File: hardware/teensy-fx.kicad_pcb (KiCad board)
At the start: 2 copper layers, 17 parts, among them J1 AudioJack3_Ground, J2 AudioJack3_Ground, U1 Teensy4.0, U2 AP7313-1.8V, U3 SGTL5000

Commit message: initial schematic and parts layout
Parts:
- added C10: 2.2u, Capacitor_SMD:C_0805_2012Metric, F.Cu at (266.1, 69.0)
- added D1: LED, LED_SMD:LED_0805_2012Metric, F.Cu at (238.1, 90.0)
- added D10: LED, LED_SMD:LED_0805_2012Metric, F.Cu at (253.1, 126.0)
- added D11: LED, LED_SMD:LED_0805_2012Metric, F.Cu at (268.1, 126.0)
- added D12: LED, LED_SMD:LED_0805_2012Metric, F.Cu at (283.0, 126.0)
- added D13: LED, LED_SMD:LED_0805_2012Metric, F.Cu at (277.0, 79.0)
- added D14: LED, LED_SMD:LED_0805_2012Metric, F.Cu at (233.0, 79.0)
- added D15: LED, LED_SMD:LED_0805_2012Metric, F.Cu at (261.1, 79.0)
- added D16: LED, LED_SMD:LED_0805_2012Metric, F.Cu at (247.9, 79.0)
- added D2: LED, LED_SMD:LED_0805_2012Metric, F.Cu at (253.0, 90.0)
- added D3: LED, LED_SMD:LED_0805_2012Metric, F.Cu at (268.0, 90.0)
- added D4: LED, LED_SMD:LED_0805_2012Metric, F.Cu at (283.0, 90.0)
- added D5: LED, LED_SMD:LED_0805_2012Metric, F.Cu at (238.0, 108.0)
- added D6: LED, LED_SMD:LED_0805_2012Metric, F.Cu at (253.0, 108.0)
- added D7: LED, LED_SMD:LED_0805_2012Metric, F.Cu at (268.0, 108.0)
- added D8: LED, LED_SMD:LED_0805_2012Metric, F.Cu at (283.0, 108.0)
- added D9: LED, LED_SMD:LED_0805_2012Metric, F.Cu at (238.0, 126.0)
- added H1: MountingHole, MountingHole:MountingHole_3.2mm_M3, F.Cu at (230.0, 50.0)
- added H2: MountingHole, MountingHole:MountingHole_3.2mm_M3, F.Cu at (280.0, 50.0)
- added H3: MountingHole, MountingHole:MountingHole_3.2mm_M3, F.Cu at (230.0, 145.0)
- added H4: MountingHole, MountingHole:MountingHole_3.2mm_M3, F.Cu at (280.0, 145.0)
- added R3: R, Resistor_SMD:R_0805_2012Metric, F.Cu at (257.0, 49.4)
- added R4: 10k, Resistor_SMD:R_0805_2012Metric, F.Cu at (262.0, 50.0)
- added RN1: R_Pack04, Resistor_SMD:R_Array_Concave_4x0603, F.Cu at (243.0, 90.0)
- added RN2: R_Pack04, Resistor_SMD:R_Array_Concave_4x0603, F.Cu at (243.0, 125.0)
- added RN3: R_Pack04, Resistor_SMD:R_Array_Concave_4x0603, F.Cu at (243.0, 78.0)
- added RN4: R_Pack04, Resistor_SMD:R_Array_Concave_4x0603, F.Cu at (243.0, 108.0)
- added RV1: R_POT, Potentiometer_THT:Potentiometer_Alps_RK09L_Single_Vertical, F.Cu at (235.0, 104.0)
- added RV10: R_POT, Potentiometer_THT:Potentiometer_Alps_RK09L_Single_Vertical, F.Cu at (250.0, 140.0)
- added RV11: R_POT, Potentiometer_THT:Potentiometer_Alps_RK09L_Single_Vertical, F.Cu at (265.0, 140.0)
- added RV12: R_POT, Potentiometer_THT:Potentiometer_Alps_RK09L_Single_Vertical, F.Cu at (280.0, 140.0)
- added RV2: R_POT, Potentiometer_THT:Potentiometer_Alps_RK09L_Single_Vertical, F.Cu at (250.0, 104.0)
- added RV3: R_POT, Potentiometer_THT:Potentiometer_Alps_RK09L_Single_Vertical, F.Cu at (265.0, 104.0)
- added RV4: R_POT, Potentiometer_THT:Potentiometer_Alps_RK09L_Single_Vertical, F.Cu at (280.0, 104.0)
- added RV5: R_POT, Potentiometer_THT:Potentiometer_Alps_RK09L_Single_Vertical, F.Cu at (235.0, 122.0)
- added RV6: R_POT, Potentiometer_THT:Potentiometer_Alps_RK09L_Single_Vertical, F.Cu at (250.0, 122.0)
- added RV7: R_POT, Potentiometer_THT:Potentiometer_Alps_RK09L_Single_Vertical, F.Cu at (265.0, 122.0)
- added RV8: R_POT, Potentiometer_THT:Potentiometer_Alps_RK09L_Single_Vertical, F.Cu at (280.0, 122.0)
- added RV9: R_POT, Potentiometer_THT:Potentiometer_Alps_RK09L_Single_Vertical, F.Cu at (235.0, 140.0)
- added SW1: Switch_SW_Push, Button_Switch_THT:SW_PUSH_6mm, F.Cu at (230.0, 82.0)
- added SW2: Switch_SW_Push, Button_Switch_THT:SW_PUSH_6mm, F.Cu at (244.0, 82.0)
- added SW3: Switch_SW_Push, Button_Switch_THT:SW_PUSH_6mm, F.Cu at (258.0, 82.0)
- added SW4: Switch_SW_Push, Button_Switch_THT:SW_PUSH_6mm, F.Cu at (274.0, 82.0)
- added U4: 4067, Package_SO:SSOP-24_5.3x8.2mm_P0.65mm, F.Cu at (273.0, 71.0)
- added U5: 74HC595, Package_SO:QSOP-16_3.9x4.9mm_P0.635mm, F.Cu at (255.0, 145.0)
- added U6: 74HC595, Package_SO:QSOP-16_3.9x4.9mm_P0.635mm, F.Cu at (255.0, 76.0)
- J1, J2: moved to B.Cu
- moved J1 135.4 mm to (279.0, 60.0), turned to 90 degrees
- moved U3 126.8 mm to (266.0, 58.0)
- moved U1 100.2 mm to (243.0, 63.0)
- moved C6 84.4 mm to (254.7, 59.3)
- moved C9 84.4 mm to (254.7, 62.2)
- moved L1 84.4 mm to (259.1, 59.3)
- moved R2 84.4 mm to (259.1, 62.2)
- moved C3 83.6 mm to (245.9, 49.7), turned to 90 degrees
- moved C1 80.7 mm to (243.9, 49.7), turned to 90 degrees
- moved U2 75.9 mm to (240.2, 49.7), turned to 90 degrees
- moved J2 75.8 mm to (231.0, 62.0), turned to 270 degrees
- moved C2 68.6 mm to (240.8, 64.4)
- moved C4 68.6 mm to (240.8, 67.3)
- moved C5 68.6 mm to (245.2, 64.4)
- moved C7 68.6 mm to (245.2, 67.3)
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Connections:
- net Net-(U1-Pad33) renamed +5V
- U1 pad 10: Net-(U1-Pad10) -> TX
- U1 pad 11: Net-(U1-Pad11) -> led_data
- U1 pad 12: Net-(U1-Pad12) -> led_clk
- U1 pad 13: Net-(U1-Pad13) -> led_latch
- U1 pad 14: Net-(U1-Pad14) -> led_oe
- U1 pad 2: Net-(U1-Pad2) -> sw_1
- U1 pad 20: Net-(U1-Pad20) -> sw_4
- U1 pad 21: Net-(U1-Pad21) -> pot_multiplex
- U1 pad 23: Net-(U1-Pad23) -> SCL
- U1 pad 24: Net-(U1-Pad24) -> SDA
- U1 pad 27: Net-(U1-Pad27) -> LRCLK
- U1 pad 28: Net-(U1-Pad28) -> BCLK
- U1 pad 3: Net-(U1-Pad3) -> sw_2
- U1 pad 31: Net-(U1-Pad31) -> +3V3
- U1 pad 32: Net-(U1-Pad32) -> GND
- U1 pad 4: Net-(U1-Pad4) -> pot_b0
- U1 pad 5: Net-(U1-Pad5) -> pot_b1
- U1 pad 6: Net-(U1-Pad6) -> pot_b2
- U1 pad 7: Net-(U1-Pad7) -> pot_b3
- U1 pad 8: Net-(U1-Pad8) -> sw_3
- U1 pad 9: Net-(U1-Pad9) -> RX
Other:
- board outline added: 60 x 105 mm

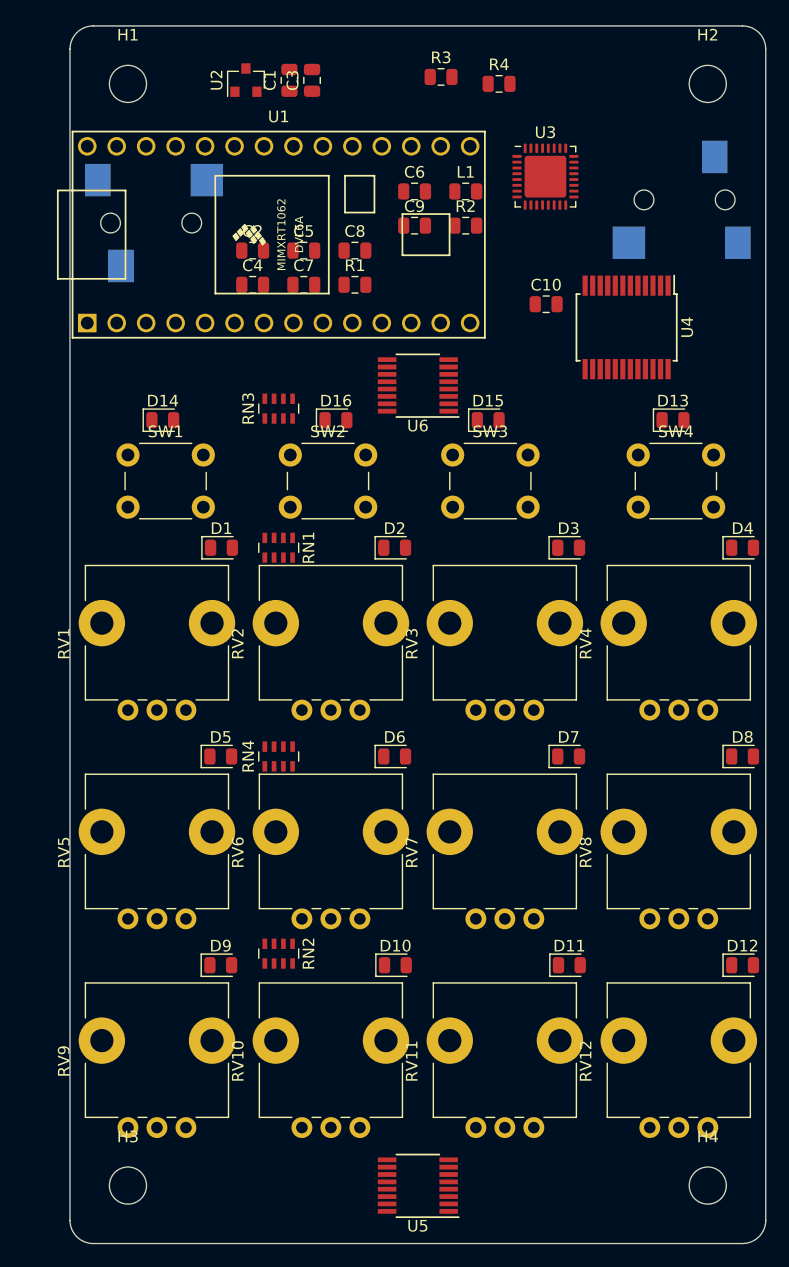
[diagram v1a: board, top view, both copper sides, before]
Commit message: switch to pwm led driver, first pass routing
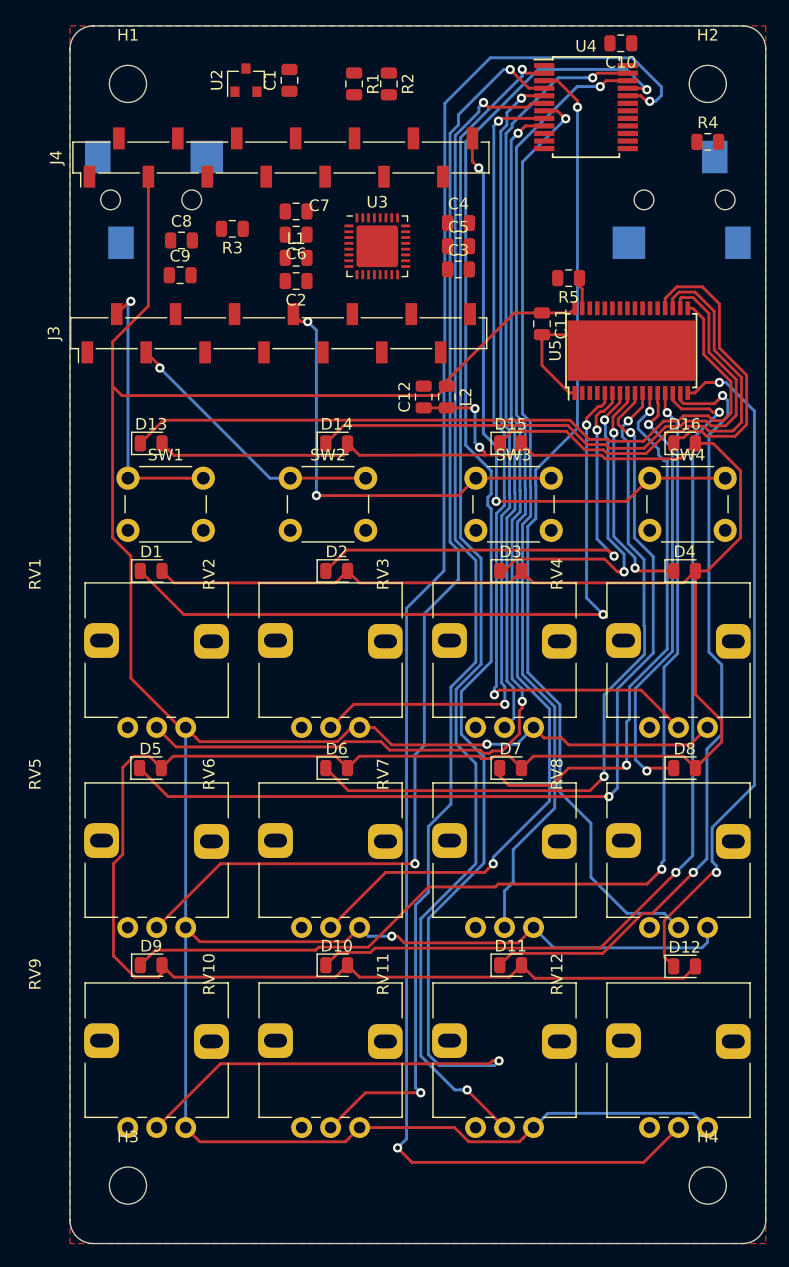
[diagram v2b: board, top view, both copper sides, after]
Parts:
- removed RN1, RN2, RN3, RN4: R_Pack04, Resistor_SMD:R_Array_Concave_4x0603
- removed U1: Teensy4.0, teensy:Teensy40
- removed U6: 74HC595, Package_SO:QSOP-16_3.9x4.9mm_P0.635mm
- added C11: 2.2uF, Capacitor_SMD:C_0805_2012Metric, F.Cu at (265.7, 70.7)
- added C12: 2.2uF, Capacitor_SMD:C_0805_2012Metric, F.Cu at (255.5, 77.0)
- added J3: Conn_01x14, Connector_PinSocket_2.54mm:PinSocket_1x14_P2.54mm_Vertical_SMD_Pin1Left, F.Cu at (243.0, 71.5)
- added J4: Conn_01x14, Connector_PinSocket_2.54mm:PinSocket_1x14_P2.54mm_Vertical_SMD_Pin1Left, F.Cu at (243.2, 56.4)
- added L2: 600R, Inductor_SMD:L_0805_2012Metric, F.Cu at (257.5, 77.0)
- added R5: 3.3k, Resistor_SMD:R_0805_2012Metric, F.Cu at (268.0, 66.8)
- C10: value 2.2u -> 2.2uF
- R3: value R -> 100R
- RV1, RV10, RV11, RV12, RV2, RV3, RV4, RV5, RV6, RV7, RV8, RV9: footprint Potentiometer_THT:Potentiometer_Alps_RK09L_Single_Vertical -> audio-fx:Potentiometer_Alps_RK09L_Single_Vertical
- U5: value 74HC595 -> TLC5947DAP; footprint Package_SO:QSOP-16_3.9x4.9mm_P0.635mm -> Package_SO:HTSSOP-32-1EP_6.1x11mm_P0.65mm_EP5.2x11mm_Mask4.11x4.36mm
- moved U5 74.3 mm to (273.4, 73.0), turned to 90 degrees
- moved J2 48.0 mm to (279.0, 60.0), turned to 90 degrees
- moved J1 48.0 mm to (231.0, 60.0), turned to 270 degrees
- moved D13 45.0 mm to (232.0, 81.0)
- moved D16 30.1 mm to (278.0, 81.0)
- moved C10 23.4 mm to (272.5, 46.5), turned to 180 degrees
- moved R3 22.3 mm to (239.0, 62.5), turned to 180 degrees
- moved C9 20.7 mm to (234.5, 66.5)
- moved C3 20.6 mm to (258.5, 66.0), turned to 0 degrees
- moved U4 19.3 mm to (269.5, 52.0), turned to 0 degrees
- moved R4 18.7 mm to (280.0, 55.0)
- moved C4 18.5 mm to (258.5, 62.0)
- moved R1 17.3 mm to (249.5, 50.0), turned to 270 degrees
- moved L1 15.7 mm to (244.5, 65.0)
- moved U3 15.7 mm to (251.5, 64.0)
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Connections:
- D1 pad 1: GND -> Net-(D1-Pad1)
- D1 pad 2: /pots/led_0 -> +3.3VA
- D10 pad 1: GND -> Net-(D10-Pad1)
- D10 pad 2: /pots/led_13 -> +3.3VA
- D11 pad 1: GND -> Net-(D11-Pad1)
- D11 pad 2: /pots/led_14 -> +3.3VA
- D12 pad 1: GND -> Net-(D12-Pad1)
- D12 pad 2: /pots/led_15 -> +3.3VA
- D13 pad 1: GND -> Net-(D13-Pad1)
- D13 pad 2: /pots/led_8 -> +3.3VA
- D14 pad 1: GND -> Net-(D14-Pad1)
- D14 pad 2: /pots/led_9 -> +3.3VA
- D15 pad 1: GND -> Net-(D15-Pad1)
- D15 pad 2: /pots/led_10 -> +3.3VA
- D16 pad 1: GND -> Net-(D16-Pad1)
- D16 pad 2: /pots/led_11 -> +3.3VA
- D2 pad 1: GND -> Net-(D2-Pad1)
- D2 pad 2: /pots/led_1 -> +3.3VA
- D3 pad 1: GND -> Net-(D3-Pad1)
- D3 pad 2: /pots/led_2 -> +3.3VA
- D4 pad 1: GND -> Net-(D4-Pad1)
- D4 pad 2: /pots/led_3 -> +3.3VA
- D5 pad 1: GND -> Net-(D5-Pad1)
- D5 pad 2: /pots/led_4 -> +3.3VA
- D6 pad 1: GND -> Net-(D6-Pad1)
- D6 pad 2: /pots/led_5 -> +3.3VA
- D7 pad 1: GND -> Net-(D7-Pad1)
- D7 pad 2: /pots/led_6 -> +3.3VA
- D8 pad 1: GND -> Net-(D8-Pad1)
- D8 pad 2: /pots/led_7 -> +3.3VA
- D9 pad 1: GND -> Net-(D9-Pad1)
- D9 pad 2: /pots/led_12 -> +3.3VA
- R3 pad 1: MCLK -> Net-(R3-Pad1)
- R3 pad 2: Net-(R3-Pad2) -> MCLK
- U3 pad 21: MCLK -> Net-(R3-Pad1)
- U5 pad 1: Net-(RN1-Pad2) -> GND
- U5 pad 10: +3V3 -> Net-(D6-Pad1)
- U5 pad 11: led_clk -> Net-(D7-Pad1)
- U5 pad 12: led_latch -> Net-(D8-Pad1)
- U5 pad 13: led_oe -> Net-(D9-Pad1)
- U5 pad 14: led_data -> Net-(D10-Pad1)
- U5 pad 15: Net-(RN1-Pad1) -> Net-(D11-Pad1)
- U5 pad 16: +3V3 -> Net-(D12-Pad1)
- U5 pad 2: Net-(RN1-Pad3) -> led_oe
- U5 pad 3: Net-(RN1-Pad4) -> led_clk
- U5 pad 4: Net-(RN2-Pad1) -> led_data
- U5 pad 5: Net-(RN2-Pad2) -> Net-(D1-Pad1)
- U5 pad 6: Net-(RN2-Pad3) -> Net-(D2-Pad1)
- U5 pad 7: Net-(RN2-Pad4) -> Net-(D3-Pad1)
- U5 pad 8: GND -> Net-(D4-Pad1)
- U5 pad 9: Net-(U5-Pad9) -> Net-(D5-Pad1)
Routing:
- net +3V3: track 0.00 -> 275.8 mm, vias 0 -> 2
- net +3.3VA: track 0.00 -> 265.0 mm, vias 0 -> 2
- net /pots/a11: track 0.00 -> 143.1 mm, vias 0 -> 2
- net /pots/a10: track 0.00 -> 142.9 mm, vias 0 -> 2
- net /pots/a3: track 0.00 -> 104.0 mm, vias 0 -> 2
- net /pots/a7: track 0.00 -> 103.4 mm, vias 0 -> 2
- net /pots/a5: track 0.00 -> 101.0 mm, vias 0 -> 2
- net /pots/a9: track 0.00 -> 93.8 mm, vias 0 -> 2
- net Net-(D9-Pad1): track 0.00 -> 90.5 mm, vias 0 -> 2
- net /pots/a0: track 0.00 -> 88.9 mm, vias 0 -> 2
- net /pots/a6: track 0.00 -> 83.9 mm, vias 0 -> 1
- net Net-(D5-Pad1): track 0.00 -> 79.9 mm, vias 0 -> 2
- net Net-(D10-Pad1): track 0.00 -> 79.8 mm, vias 0 -> 2
- net /pots/a2: track 0.00 -> 76.9 mm, vias 0 -> 1
- net /pots/a1: track 0.00 -> 71.8 mm, vias 0 -> 2
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- added copper zone on F.Cu, net GND

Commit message: tidy schematic and finish layout
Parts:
- moved C9 0.75 mm to (234.5, 65.8), turned to 180 degrees
- moved D1 0.30 mm to (232.0, 91.7)
- moved D2 0.30 mm to (248.0, 91.7)
- moved D3 0.30 mm to (263.0, 91.7)
- moved D4 0.30 mm to (278.0, 91.7)
- moved C8 0.12 mm to (234.5, 63.5), turned to 180 degrees
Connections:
- net /pots/a0 renamed /pots buttons & LEDs/a0
- net /pots/a1 renamed /pots buttons & LEDs/a1
- net /pots/a10 renamed /pots buttons & LEDs/a10
- net /pots/a11 renamed /pots buttons & LEDs/a11
- net /pots/a2 renamed /pots buttons & LEDs/a2
- net /pots/a3 renamed /pots buttons & LEDs/a3
- net /pots/a4 renamed /pots buttons & LEDs/a4
- net /pots/a5 renamed /pots buttons & LEDs/a5
- net /pots/a6 renamed /pots buttons & LEDs/a6
- net /pots/a7 renamed /pots buttons & LEDs/a7
- net /pots/a8 renamed /pots buttons & LEDs/a8
- net /pots/a9 renamed /pots buttons & LEDs/a9
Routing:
- net GND: track 14.7 -> 152.3 mm, vias 0 -> 122
- net +3V3: track 275.8 -> 374.6 mm, vias 2 -> 4
- net pot_b3: track 0.00 -> 73.2 mm, vias 0 -> 2
- net pot_b2: track 0.00 -> 64.1 mm, vias 0 -> 2
- net pot_b0: track 0.00 -> 56.8 mm, vias 0 -> 2
- net pot_b1: track 0.00 -> 56.2 mm, vias 0 -> 2
- net Net-(J2-PadS): track 0.00 -> 47.3 mm, vias 0 -> 3
- net Net-(J2-PadR): track 0.00 -> 44.5 mm, vias 0 -> 3
- net Net-(J2-PadT): track 0.00 -> 42.4 mm, vias 0 -> 3
- net Net-(R3-Pad1): track 0.00 -> 30.1 mm, vias 0 -> 4
- net BCLK: track 0.00 -> 28.9 mm, vias 0 -> 2
- net led_clk: track 0.00 -> 27.5 mm, vias 0 -> 2
- net led_latch: track 0.00 -> 27.2 mm, vias 0 -> 2
- net led_data: track 0.00 -> 25.6 mm, vias 0 -> 2
- net LRCLK: track 0.00 -> 24.9 mm, vias 0 -> 2
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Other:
- outline, holes or cut-outs redrawn

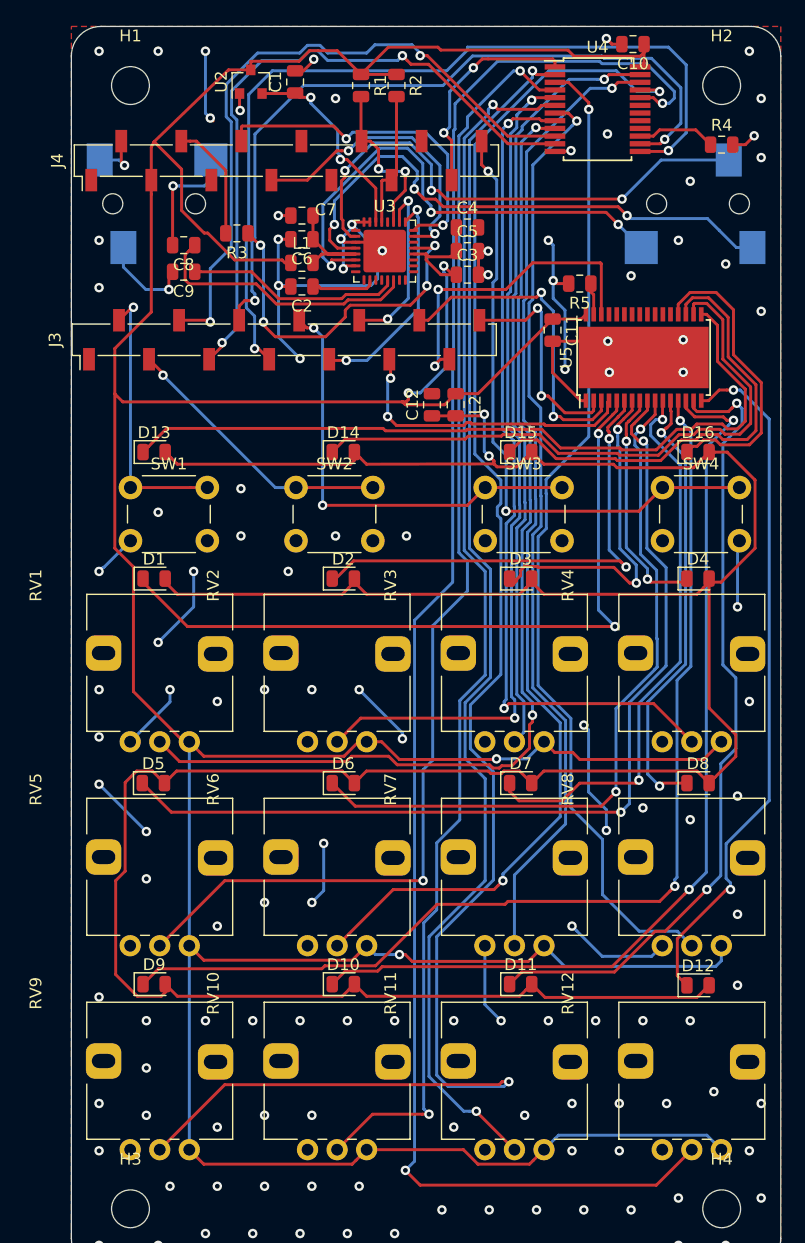
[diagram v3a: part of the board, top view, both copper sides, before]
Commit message: made better fp for smt teensy, fixed some wiring errors
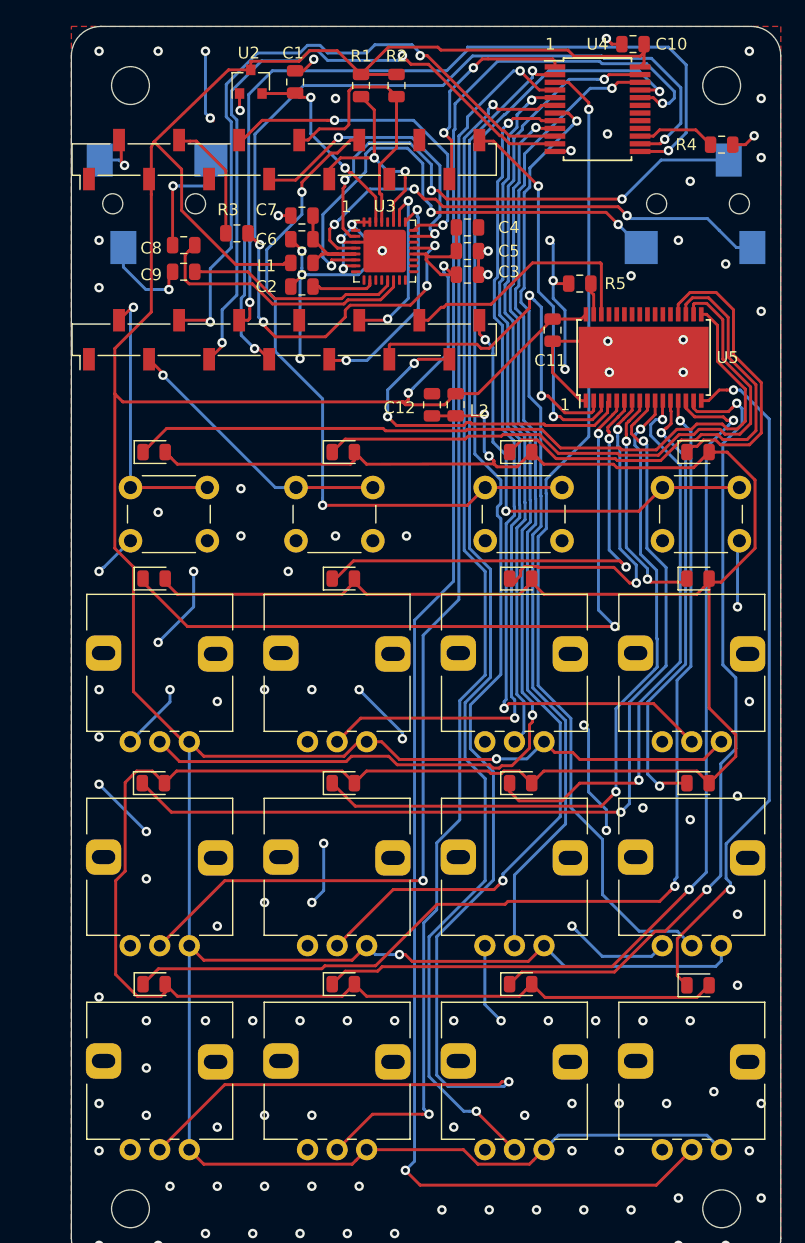
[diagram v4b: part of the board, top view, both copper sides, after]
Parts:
- removed J3, J4: Conn_01x14, Connector_PinSocket_2.54mm:PinSocket_1x14_P2.54mm_Vertical_SMD_Pin1Left
- added U1: Teensy4.0, audio-fx:teensy4smt, F.Cu at (243.0, 71.5)
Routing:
- net sw_3: track 37.7 -> 57.7 mm
- net sw_4: track 53.0 -> 37.7 mm
- net SCL: track 11.6 -> 23.5 mm
- net led_oe: track 18.8 -> 30.7 mm
- net led_latch: track 27.2 -> 21.7 mm, vias 2 -> 0
- net Net-(J2-PadS): track 47.3 -> 42.6 mm
- net GND: track 152.3 -> 147.7 mm
- net SDA: track 14.2 -> 18.5 mm
- net led_clk: track 27.5 -> 31.7 mm
- net led_data: track 25.6 -> 29.2 mm
- net BCLK: track 28.9 -> 28.2 mm
- net /pots buttons & LEDs/a5: track 101.0 -> 100.4 mm
- net /pots buttons & LEDs/a1: track 72.0 -> 72.6 mm
- net /pots buttons & LEDs/a9: track 93.9 -> 94.5 mm
- net /pots buttons & LEDs/a8: track 65.4 -> 66.0 mm
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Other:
- board text added: "1"
